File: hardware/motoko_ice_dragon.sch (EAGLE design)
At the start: 119 parts, among them IC2 LM2937, Q1 8MHz, Q10 20mA/30V, Q11 20mA/30V, Q2 BSS138TOP, Q3 BSS138TOP, Q4 20mA/30V, Q5 20mA/30V, Q6 20mA/30V, Q7 20mA/30V, Q8 20mA/30V, Q9 20mA/30V, U1 MP6540HA, U2 STM32_STM32F722XX, U3 MP6540HA

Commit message: main board
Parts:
- removed C10, C12: 10uF, resistor:C-EUC0805
- removed C11, C9: 100n, resistor:C-EUC0805
- removed IC2: LM2937, linear:LM2937
- added C39, C41, C42: 100n, resistor:C-EUC0805
- added C40, C43, C44: 10uF, resistor:C-EUC0805
- added L1: 4.7uH, TYS50204R7N-10, SparkFun-Coils:INDUCTOR-CR54-3.3UH
- added U4: AP63203, SparkFun-IC-Power:AP63203
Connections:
- new net N$22: C39.2, U4.BST
- new net N$26: C39.1, L1.1, U4.SW
- net +3V3: now also C42.2, C43.2, C44.2, L1.2, U4.FB; no longer C11.1, C12.1, IC2.VO
- net GND: now also C40.1, C41.1, C42.1, C43.1, C44.1, U4.GND; no longer C10.2, C11.2, C12.2, C9.2, IC2.GND
- net VCC: now also C40.2, C41.2, U4.EN, U4.VIN; no longer C10.1, C9.1, IC2.VI
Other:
- moved on the sheet: C17, C18, C27, C32, C33, C34, C35, C36, C37, C38, C4, C7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

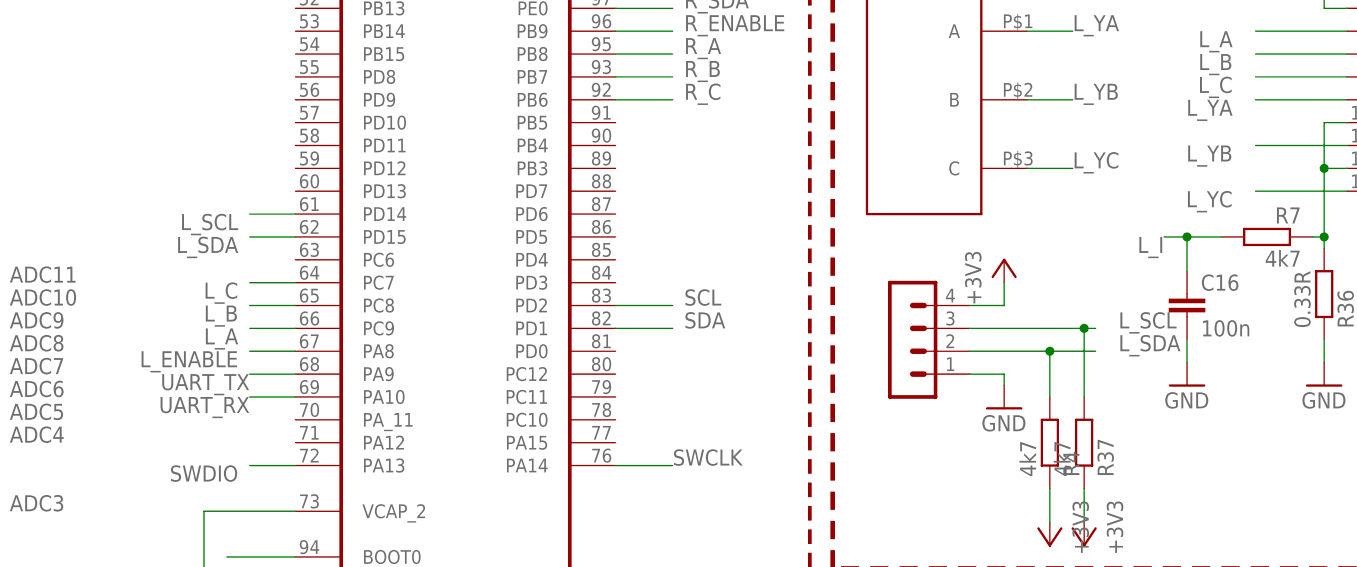
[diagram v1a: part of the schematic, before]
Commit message: identification, sensors calibrations
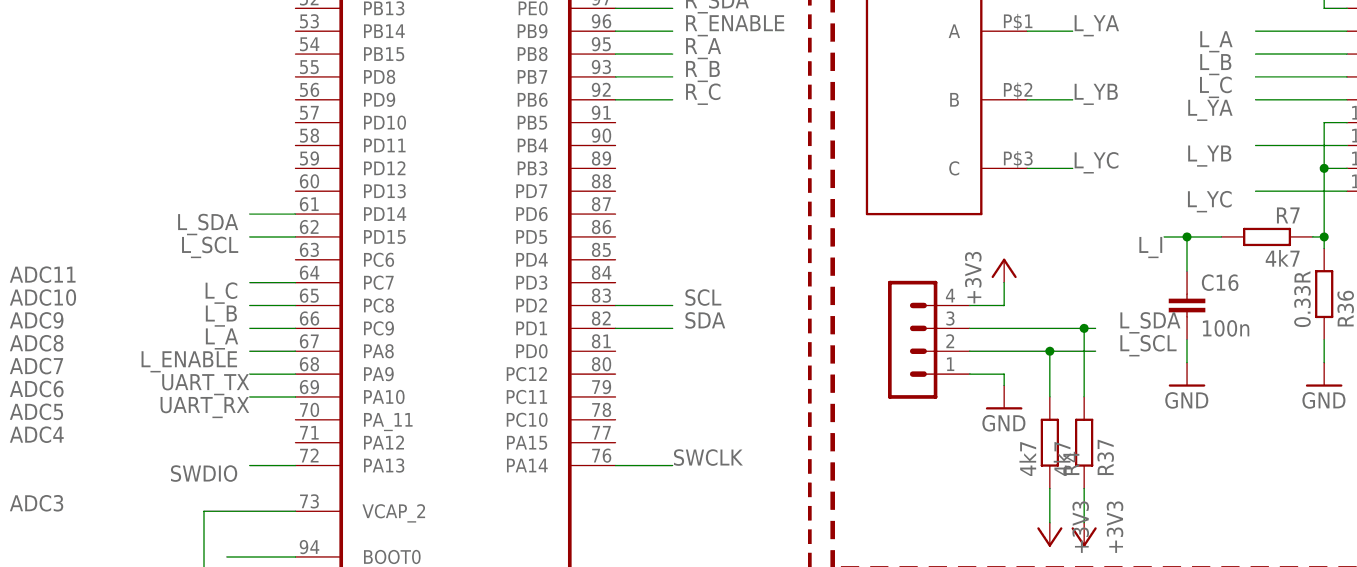
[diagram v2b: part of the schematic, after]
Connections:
- net L_SCL: now also L_ENCODER.2, R4.2, U2B.PD15; no longer L_ENCODER.3, R37.2, U2B.PD14
- net L_SDA: now also L_ENCODER.3, R37.2, U2B.PD14; no longer L_ENCODER.2, R4.2, U2B.PD15
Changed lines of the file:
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@@
-</segment>
-</net>
-<net name="L_SCL" class="0">
-<segment>
-<pinref part="L_ENCODER" gate="1" pin="3"/>
-<wire x1="185.42" y1="210.82" x2="198.12" y2="210.82" width="0.1524" layer="91"/>
-<label x="201.93" y="210.82" size="1.778" layer="95"/>
-<pinref part="R37" gate="G$1" pin="2"/>
-<wire x1="198.12" y1="210.82" x2="199.39" y2="210.82" width="0.1524" layer="91"/>
-<wire x1="198.12" y1="203.2" x2="198.12" y2="210.82" width="0.1524" layer="91"/>
-<junction x="198.12" y="210.82"/>
-</segment>
-<segment>
-<pinref part="U2" gate="B" pin="PD14"/>
-<wire x1="110.49" y1="223.52" x2="105.41" y2="223.52" width="0.1524" layer="91"/>
-<label x="104.14" y="223.52" size="1.778" layer="95" rot="R180"/>
-</segment>
-</net>
-<net name="L_SDA" class="0">
-<segment>
-<pinref part="L_ENCODER" gate="1" pin="2"/>
-<wire x1="185.42" y1="208.28" x2="194.31" y2="208.28" width="0.1524" layer="91"/>
-<label x="201.93" y="208.28" size="1.778" layer="95"/>
-<pinref part="R4" gate="G$1" pin="2"/>
-<wire x1="194.31" y1="208.28" x2="199.39" y2="208.28" width="0.1524" layer="91"/>
-<wire x1="194.31" y1="203.2" x2="194.31" y2="208.28" width="0.1524" layer="91"/>
-<junction x="194.31" y="208.28"/>
-</segment>
-<segment>
-<pinref part="U2" gate="B" pin="PD15"/>
-<wire x1="110.49" y1="220.98" x2="105.41" y2="220.98" width="0.1524" layer="91"/>
-<label x="104.14" y="220.98" size="1.778" layer="95" rot="R180"/>
 </segment>
 </net>
@@
 </segment>
 </net>
+<net name="L_SDA" class="0">
+<segment>
+<pinref part="U2" gate="B" pin="PD14"/>
+<wire x1="110.49" y1="223.52" x2="105.41" y2="223.52" width="0.1524" layer="91"/>
+<label x="104.14" y="223.52" size="1.778" layer="95" rot="R180"/>
+</segment>
+<segment>
+<pinref part="L_ENCODER" gate="1" pin="3"/>
+<wire x1="185.42" y1="210.82" x2="198.12" y2="210.82" width="0.1524" layer="91"/>
+<label x="201.93" y="210.82" size="1.778" layer="95"/>
+<pinref part="R37" gate="G$1" pin="2"/>
+<wire x1="198.12" y1="210.82" x2="199.39" y2="210.82" width="0.1524" layer="91"/>
+<wire x1="198.12" y1="203.2" x2="198.12" y2="210.82" width="0.1524" layer="91"/>
+<junction x="198.12" y="210.82"/>
+</segment>
+</net>
+<net name="L_SCL" class="0">
+<segment>
+<pinref part="U2" gate="B" pin="PD15"/>
+<wire x1="110.49" y1="220.98" x2="105.41" y2="220.98" width="0.1524" layer="91"/>
+<label x="104.14" y="220.98" size="1.778" layer="95" rot="R180"/>
+</segment>
+<segment>
+<pinref part="L_ENCODER" gate="1" pin="2"/>
+<wire x1="185.42" y1="208.28" x2="194.31" y2="208.28" width="0.1524" layer="91"/>
+<label x="201.93" y="208.28" size="1.778" layer="95"/>
+<pinref part="R4" gate="G$1" pin="2"/>
+<wire x1="194.31" y1="208.28" x2="199.39" y2="208.28" width="0.1524" layer="91"/>
+<wire x1="194.31" y1="203.2" x2="194.31" y2="208.28" width="0.1524" layer="91"/>
+<junction x="194.31" y="208.28"/>
+</segment>
+</net>

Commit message: board rev 2
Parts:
- removed C14: 10n, resistor:C-EUC0805
- removed LSM6DS1: ST_L3GD20H, motoko_5_0:ST_L3GD20H
- added C9: 100n, resistor:C-EUC0805
- added FD1, FD2, FD3, FD4, FD5, FD6, FD7, FD8, FD9: FIDUCIAL1X2, SparkFun-Aesthetics:FIDUCIAL1X2
- added JP2: boot, jumper:JP1E
- added LED10: (no value), led:LEDCHIPLED_1206
- added R38: 330, resistor:R-EU_M0805
- added R39: 4k7, resistor:R-EU_M0805
- added R42, R43: 4k7, rcl:R-EU_M0805
- added U$3: LSM6DSM, my_library:LSM6DSM
- added U$4: 24LC24_SOT23, my_library:24LC24_SOT23
- R1, R36: device resistor:R-EU_M0805 -> rcl:R-EU_M1206
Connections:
- removed net N$6: C14.2, LSM6DS1.CAP
- new net LED_2: R9.2, U2A.PE2
- new net LED_3: R38.2, U2B.PD13
- new net MEM_SCL: R42.2, U$4.SCL, U2B.PD4
- new net MEM_SDA: R43.2, U$4.SDA, U2B.PD3
- new net N$11: LED10.A, R38.1
- net +3V3: now also C9.1, JP2.2, R42.1, R43.1, U$3.CS, U$3.VDD, U$3.VDDIO, U$4.VCC; no longer LSM6DS1.CS, LSM6DS1.VDD, LSM6DS1.VDD_IO, R9.2
- net BOOT: now also JP2.1, R39.2
- net GND: now also C9.2, LED10.C, LED9.C, R39.1, U$3.GND1, U$3.GND2, U$3.SCX, U$3.SDO/SA0, U$3.SDX, U$4.GND, U$4.WP; no longer C14.1, LSM6DS1.DEN, LSM6DS1.GND, LSM6DS1.RES1, LSM6DS1.RES2, LSM6DS1.RES3, LSM6DS1.RES4, LSM6DS1.SDO
- net KEY: now also U2A.PE4; no longer U2A.PE3
- net LED_1: now also U2A.PE3; no longer U2A.PE2
- net LINE_LED: no longer LED9.C
- net SCL: now also U$3.SCL; no longer LSM6DS1.SCL/SPC
- net SDA: now also U$3.SDA; no longer LSM6DS1.SDA/SDI
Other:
- moved on the sheet: C26, LED9, R9

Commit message: gyro tests
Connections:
- net L_SCL: now also L_ENCODER.3, R37.2, U2B.PD14; no longer L_ENCODER.2, R4.2, U2B.PD15
- net L_SDA: now also L_ENCODER.2, R4.2, U2B.PD15; no longer L_ENCODER.3, R37.2, U2B.PD14
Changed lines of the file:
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@@
 </segment>
 </net>
-<net name="L_SDA" class="0">
-<segment>
-<pinref part="U2" gate="B" pin="PD14"/>
-<wire x1="110.49" y1="223.52" x2="105.41" y2="223.52" width="0.1524" layer="91"/>
-<label x="104.14" y="223.52" size="1.778" layer="95" rot="R180"/>
-</segment>
+<net name="L_SCL" class="0">
 <segment>
 <pinref part="L_ENCODER" gate="1" pin="3"/>
@@
 <junction x="198.12" y="210.82"/>
 </segment>
-</net>
-<net name="L_SCL" class="0">
 <segment>
-<pinref part="U2" gate="B" pin="PD15"/>
-<wire x1="110.49" y1="220.98" x2="105.41" y2="220.98" width="0.1524" layer="91"/>
-<label x="104.14" y="220.98" size="1.778" layer="95" rot="R180"/>
-</segment>
-<segment>
-<pinref part="L_ENCODER" gate="1" pin="2"/>
-<wire x1="185.42" y1="208.28" x2="194.31" y2="208.28" width="0.1524" layer="91"/>
-<label x="201.93" y="208.28" size="1.778" layer="95"/>
-<pinref part="R4" gate="G$1" pin="2"/>
-<wire x1="194.31" y1="208.28" x2="199.39" y2="208.28" width="0.1524" layer="91"/>
-<wire x1="194.31" y1="203.2" x2="194.31" y2="208.28" width="0.1524" layer="91"/>
-<junction x="194.31" y="208.28"/>
+<pinref part="U2" gate="B" pin="PD14"/>
+<wire x1="110.49" y1="223.52" x2="105.41" y2="223.52" width="0.1524" layer="91"/>
+<label x="104.14" y="223.52" size="1.778" layer="95" rot="R180"/>
 </segment>
 </net>
@@
 </segment>
 </net>
+<net name="L_SDA" class="0">
+<segment>
+<pinref part="L_ENCODER" gate="1" pin="2"/>
+<wire x1="185.42" y1="208.28" x2="194.31" y2="208.28" width="0.1524" layer="91"/>
+<label x="201.93" y="208.28" size="1.778" layer="95"/>
+<pinref part="R4" gate="G$1" pin="2"/>
+<wire x1="194.31" y1="208.28" x2="199.39" y2="208.28" width="0.1524" layer="91"/>
+<wire x1="194.31" y1="203.2" x2="194.31" y2="208.28" width="0.1524" layer="91"/>
+<junction x="194.31" y="208.28"/>
+</segment>
+<segment>
+<pinref part="U2" gate="B" pin="PD15"/>
+<wire x1="110.49" y1="220.98" x2="105.41" y2="220.98" width="0.1524" layer="91"/>
+<label x="104.14" y="220.98" size="1.778" layer="95" rot="R180"/>
+</segment>
+</net>
